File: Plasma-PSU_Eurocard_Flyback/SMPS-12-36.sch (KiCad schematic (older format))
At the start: 0 parts

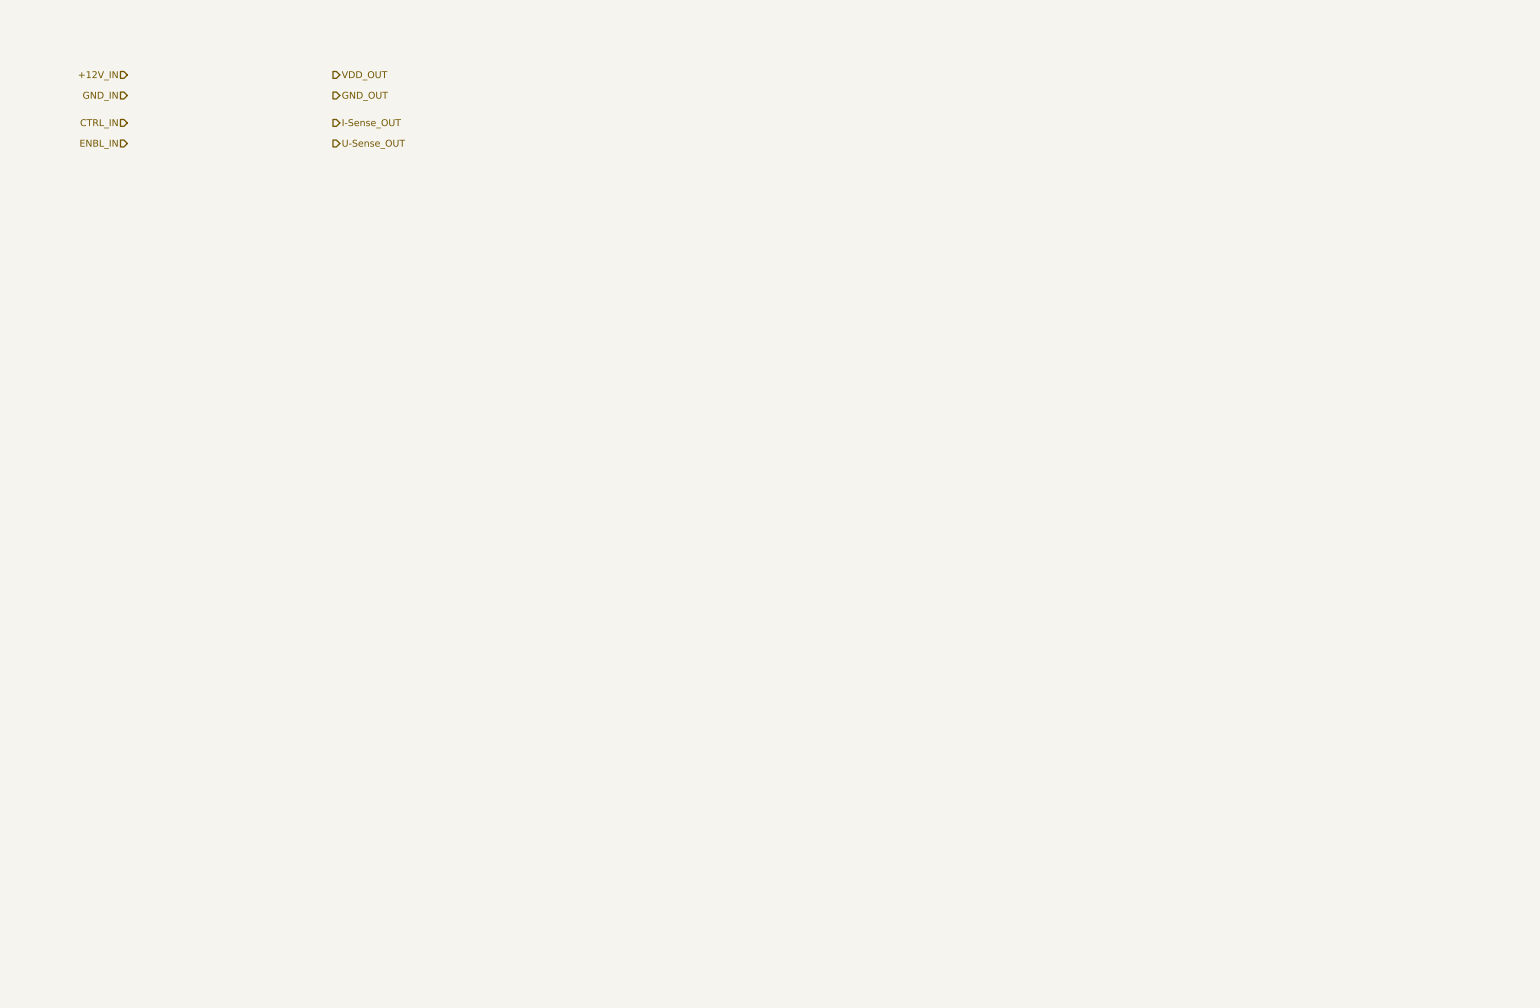
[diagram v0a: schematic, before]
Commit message: Include LTC3786 regulator IC
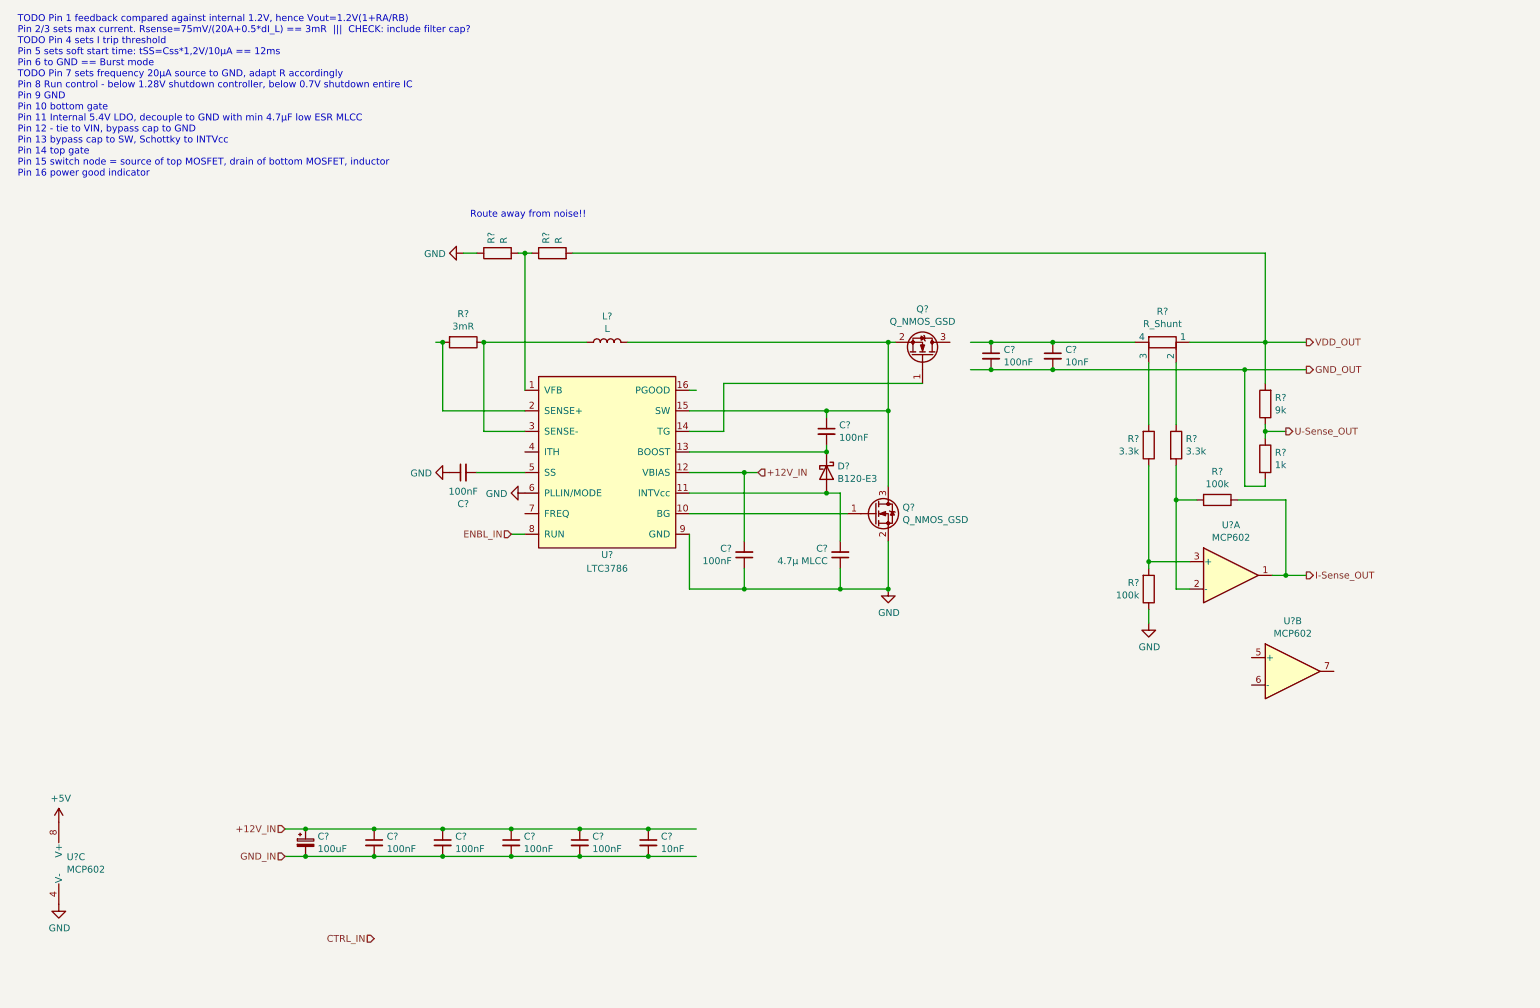
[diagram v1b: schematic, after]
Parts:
- added C? (x8): 100nF, symbol Device:C_Small
- added C?: 100uF, symbol Device:CP_Small
- added C? (x2): 10nF, symbol Device:C_Small
- added C?: 4.7µ MLCC, symbol Device:C_Small
- added D?: B120-E3, Diode_SMD:D_SMA, symbol Diode:B120-E3
- added L?: L, symbol Device:L
- added Q? (x2): Q_NMOS_GSD, symbol Device:Q_NMOS_GSD
- added R?: 9k, symbol Device:R
- added R?: 1k, symbol Device:R
- added R?: R_Shunt, symbol Device:R_Shunt
- added R? (x2): 3.3k, symbol Device:R
- added R? (x2): 100k, symbol Device:R
- added R?: 3mR, symbol Device:R
- added R? (x2): R, symbol Device:R
- added U? (x3): MCP602, symbol Amplifier_Operational:MCP602
- added U?: LTC3786, symbol Regulator_Switching:LTC3786
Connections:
- net labels added: +5V, GND
- wire segments 0 -> 85
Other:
- note added: "Route away from noise!!"
- note added: "TODO Pin 1 feedback compared against internal 1.2V, hence Vout=1.2V(1+RA/RB)\nPin 2/3 sets max current. Rsense=75mV/(20A+0.5*dI_L) == 3mR ||| CHECK: include filter cap?\nTODO Pin 4 sets I trip threshold\nPin 5 sets soft start time: tSS=Css*1,2V/10µA == 12ms\nPin 6 to GND == Burst mode\nTODO Pin 7 sets frequency 20µA source to GND, adapt R accordingly\nPin 8 Run control - below 1.28V shutdown cont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"

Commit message: LTC3786 arranged according to datasheet
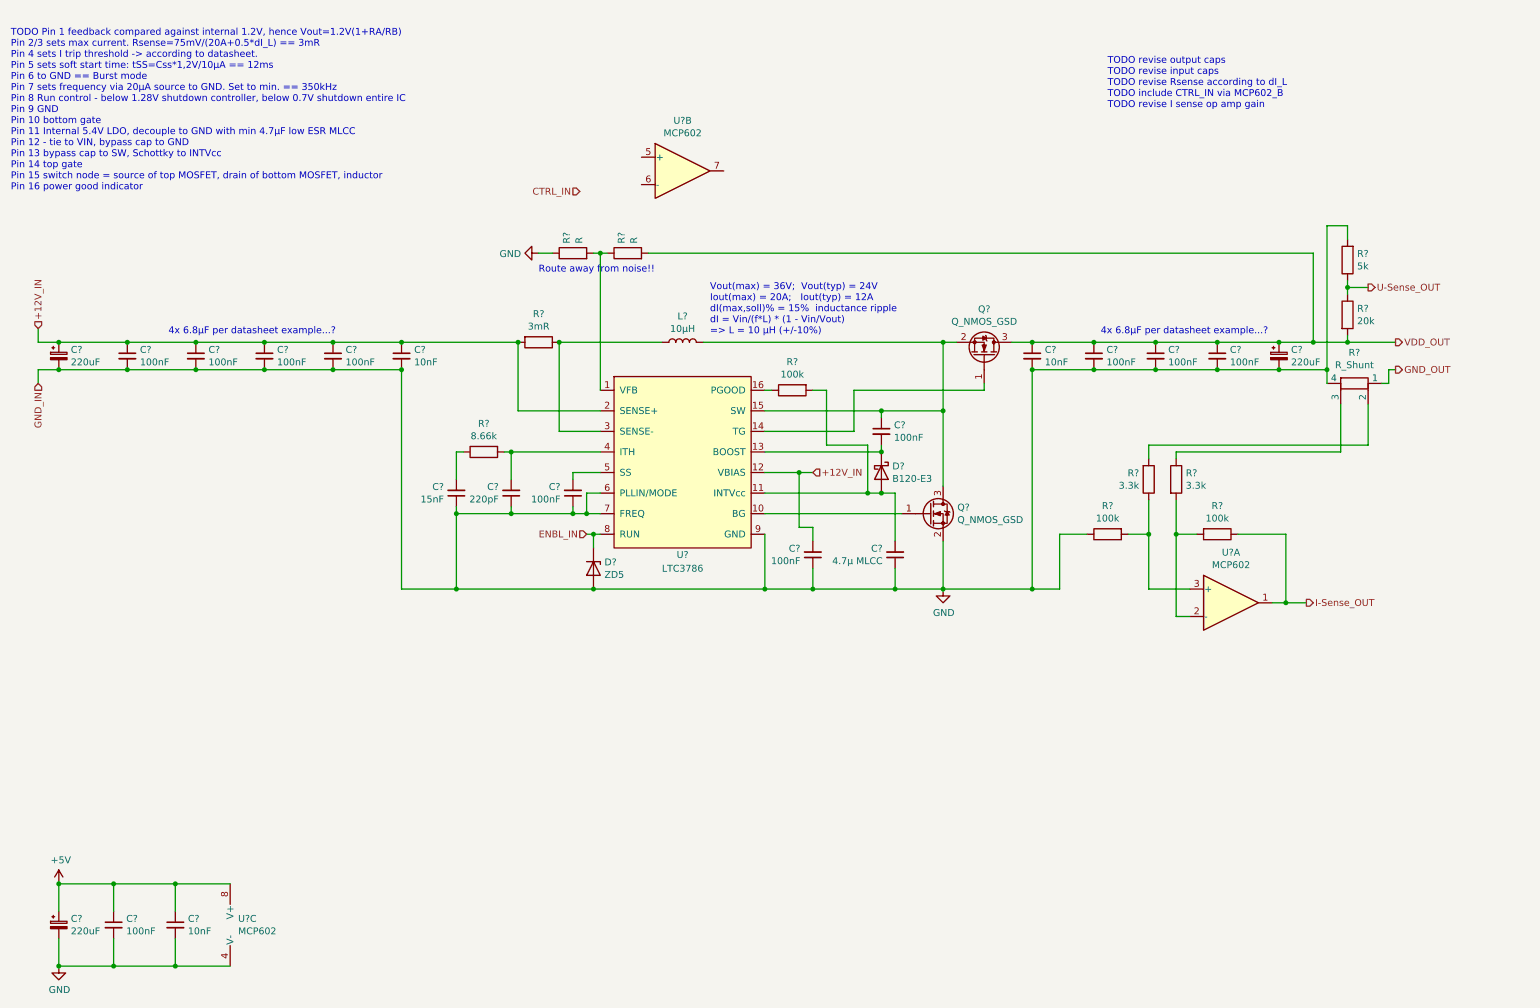
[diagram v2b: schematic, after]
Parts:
- added C? (x3): 100nF, symbol Device:C_Small
- added C? (x2): 220uF, symbol Device:CP_Small
- added C?: 15nF, symbol Device:C_Small
- added C?: 220pF, symbol Device:C_Small
- added C?: 10nF, symbol Device:C_Small
- added D?: ZD5, symbol Device:D_Zener
- added R?: 100k, symbol Device:R
- added R?: 8.66k, symbol Device:R
- C?: value 100uF -> 220uF
- L?: value L -> 10µH
- R?: value 9k -> 5k
- R?: value 1k -> 20k
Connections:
- wire segments 85 -> 144
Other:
- note added: "4x 6.8µF per datasheet example...?"
- note added: "TODO Pin 1 feedback compared against internal 1.2V, hence Vout=1.2V(1+RA/RB)\nPin 2/3 sets max current. Rsense=75mV/(20A+0.5*dI_L) == 3mR \nPin 4 sets I trip threshold -> according to datasheet.\nPin 5 sets soft start time: tSS=Css*1,2V/10µA == 12ms\nPin 6 to GND == Burst mode\nPin 7 sets frequency via 20µA source to GND. Set to min. == 350kHz\nPin 8 Run control - below 1.28V shutdown controller,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"
- note added: "TODO revise output caps\nTODO revise input caps\nTODO revise Rsense according to dI_L\nTODO include CTRL_IN via MCP602_B\nTODO revise I sense op amp gain"
- note added: "Vout(max) = 36V; Vout(typ) = 24V\nIout(max) = 20A; Iout(typ) = 12A\ndI(max,soll)% = 15% inductance ripple\ndI = Vin/(f*L) * (1 - Vin/Vout)\n=> L = 10 µH (+/-10%)"
- note removed: "TODO Pin 1 feedback compared against internal 1.2V, hence Vout=1.2V(1+RA/RB)\nPin 2/3 sets max current. Rsense=75mV/(20A+0.5*dI_L) == 3mR ||| CHECK: include filter cap?\nTODO Pin 4 sets I trip threshold\nPin 5 sets soft start time: tSS=Css*1,2V/10µA == 12ms\nPin 6 to GND == Burst mode\nTODO Pin 7 sets frequency 20µA source to GND, adapt R accordingly\nPin 8 Run control - below 1.28V shutdown cont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"
- moved on the sheet: C?, D?, L?, Q?, R?, U?, U?A, U?B, U?C
